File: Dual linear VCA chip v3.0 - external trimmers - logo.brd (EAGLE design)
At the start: 22.7 x 17.8 mm, 21 parts, among them IC1 LM13700M, IC2 TL072D, IC3 TL072D, Q1 MMBT3906LT1SMD, Q2 MMBT3906LT1SMD

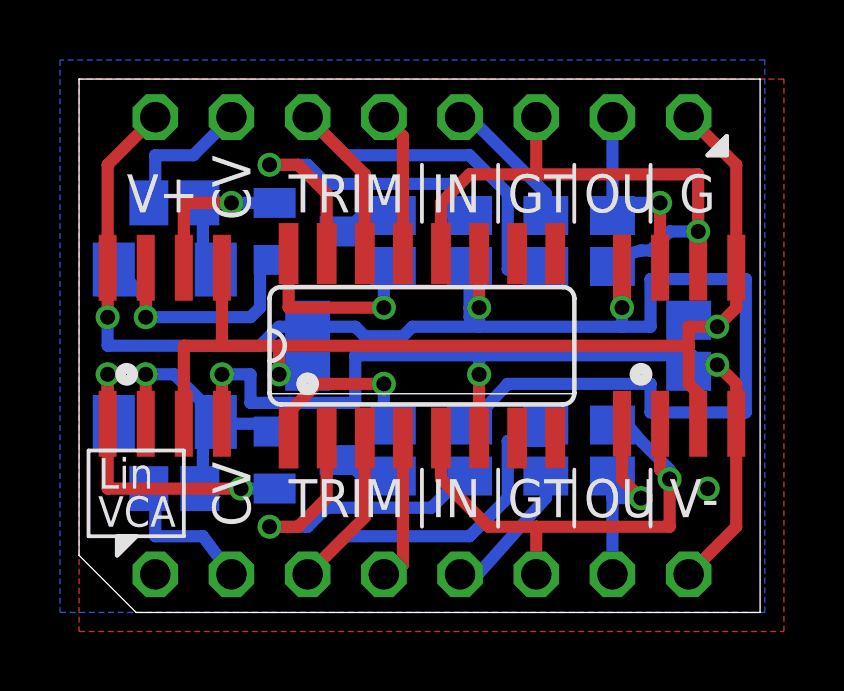
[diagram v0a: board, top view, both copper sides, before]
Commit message: Routed v2164-based quad VCA
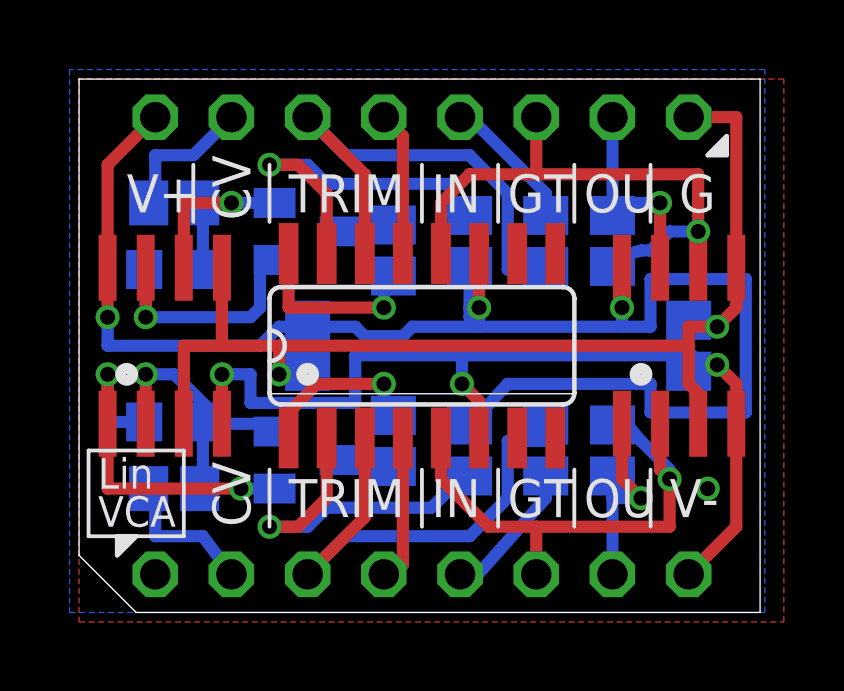
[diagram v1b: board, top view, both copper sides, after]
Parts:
- D1, D2: value (none) -> 1N41480805; device diode:SOD80C -> joakim:D0805-J
- moved R6 0.32 mm to (10.5, 12.1)
- moved D1 0.32 mm to (3.17, 6.35), turned to 180 degrees
- moved D2 0.32 mm to (3.17, 11.4), turned to 180 degrees
- moved R5 0.32 mm to (10.5, 5.71)
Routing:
- net N$10: track 12.2 -> 13.3 mm
- net GND: track 37.4 -> 38.3 mm
- net N$1: track 2.48 -> 1.89 mm
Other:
- board text removed: "C3"
- board text removed: "C4"
